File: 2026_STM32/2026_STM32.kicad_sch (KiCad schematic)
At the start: 15 parts, among them J1 USB_B, J2 Conn_ARM_SWD_TagConnect_TC2030, SW1 1825910-6, U1 STM32C011J4Mx, U2 XC6206P332MR, U3 KTD2026

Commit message: Redo schematic for 20 pin STM and adding more LEDs
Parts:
- removed C4: 100n, Capacitor_SMD:C_0603_1608Metric_Pad1.08x0.95mm_HandSolder, symbol Device:C
- removed C5: C, Capacitor_SMD:C_0603_1608Metric_Pad1.08x0.95mm_HandSolder, symbol Device:C
- removed D2: BLUE, Diode_SMD:D_1206_3216Metric_Pad1.42x1.75mm_HandSolder, symbol Device:LED
- removed J2: Conn_ARM_SWD_TagConnect_TC2030, Connector:Tag-Connect_TC2030-IDC-FP_2x03_P1.27mm_Vertical, symbol Connector:Conn_ARM_SWD_TagConnect_TC2030
- removed R1: 100R, Capacitor_SMD:C_0603_1608Metric_Pad1.08x0.95mm_HandSolder, symbol Device:R_US
- removed RV1: TC33X-2-203E, Potentiometer_SMD:Potentiometer_Bourns_TC33X_Vertical, symbol Device:R_Potentiometer
- removed SW1: 1825910-6, Button_Switch_THT:SW_PUSH_6mm, symbol Switch:SW_Push
- removed U1: STM32C011J4Mx, Package_SO:SOIC-8_3.9x4.9mm_P1.27mm, symbol MCU_ST_STM32C0:STM32C011J4Mx
- added C6: 100nF, Capacitor_SMD:C_0603_1608Metric_Pad1.08x0.95mm_HandSolder, symbol Device:C
- added C7: 4.7uF, Capacitor_SMD:C_0603_1608Metric_Pad1.08x0.95mm_HandSolder, symbol Device:C
- added D3: RED, Diode_SMD:D_1206_3216Metric_Pad1.42x1.75mm_HandSolder, symbol Device:LED
- added D4: GREEN, Diode_SMD:D_1206_3216Metric_Pad1.42x1.75mm_HandSolder, symbol Device:LED
- added D5: BLUE, Diode_SMD:D_1206_3216Metric_Pad1.42x1.75mm_HandSolder, symbol Device:LED
- added J3: Conn_01x05_Pin, symbol Connector:Conn_01x05_Pin
- added R2: 10kR, Capacitor_SMD:C_0603_1608Metric_Pad1.08x0.95mm_HandSolder, symbol Device:R_US
- added R3, R4, R5: 100R, Capacitor_SMD:C_0603_1608Metric_Pad1.08x0.95mm_HandSolder, symbol Device:R_US
- added RV2: TC33X-2-203E, Potentiometer_SMD:Potentiometer_Bourns_TC33X_Vertical, symbol Device:R_Potentiometer
- added SW2: 1825910-6, Button_Switch_THT:SW_PUSH_6mm, symbol Switch:SW_Push
- added U4: STM32C011F4P6, Package_SO:TSSOP-20_4.4x6.5mm_P0.65mm, symbol MCU_ST_STM32C0:STM32C011F4Px
- C3: value 100n -> 1.0uF
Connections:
- net +3V3: now also C6.1, C7.1, J3.1 (Pin_1), RV2.1, SW2.2, U4.4 (VDD)
- net GND: now also C6.2, C7.2, J3.5 (Pin_5), R2.2, R3.2, R4.2, R5.2, RV2.3, U4.5 (VSS)
- net SCL: now also U4.20 (PB6)
- net SDA: now also U4.1 (PB7)
- net SWDIO: now also J3.4 (Pin_4), U4.18 (PA13)
- net ~{RST}: now also J3.2 (Pin_2), U4.6 (PF2)
- new net: R2.1, SW2.1, U4.8 (PA1)
- new net: RV2.2, U4.7 (PA0)
- new net: D4.1 (K), R4.1
- new net: D5.1 (K), R5.1
- new net: D3.1 (K), R3.1
- new net BLUE: D5.2 (A), U4.11 (PA4)
- new net GREEN: D4.2 (A), U4.10 (PA3)
- new net RED: D3.2 (A), U4.9 (PA2)
- new net SWCLK: J3.3 (Pin_3), U4.19 (PA14)
- no-connect marks 4 -> 11
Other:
- company: (none) -> Waterloo Rocketry
- title: (none) -> 2026 Tutorial Board
- moved on the sheet: C3, D1, U3

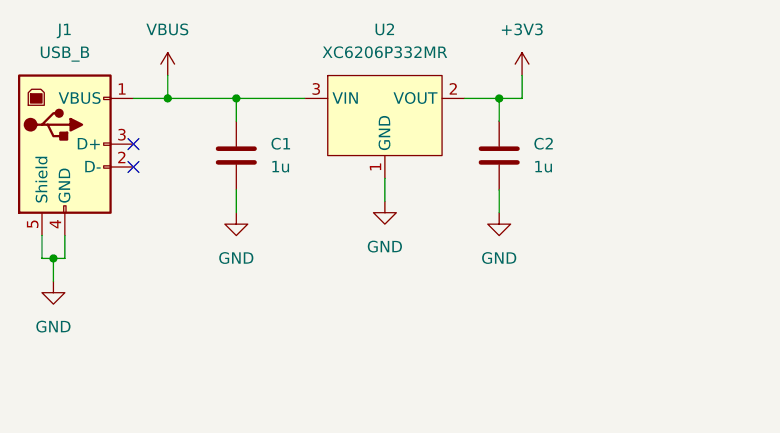
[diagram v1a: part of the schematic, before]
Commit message: Change LDO to SPX3819 (Existing Standard LDO)
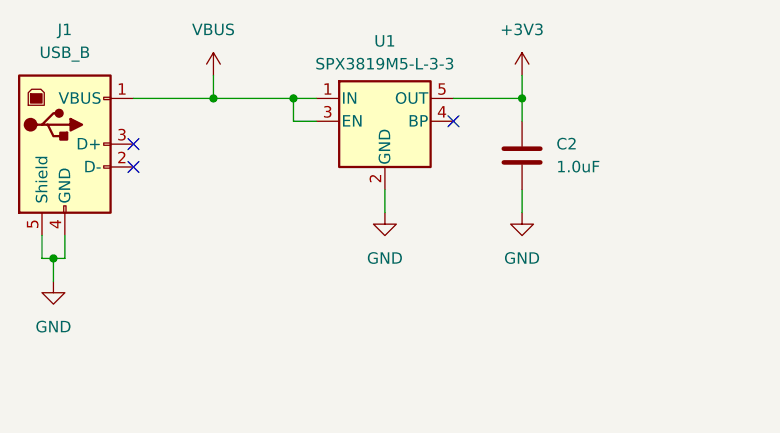
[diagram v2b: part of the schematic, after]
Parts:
- removed C1: 1u, Capacitor_SMD:C_0603_1608Metric_Pad1.08x0.95mm_HandSolder, symbol Device:C
- removed U2: XC6206P332MR, Package_TO_SOT_SMD:SOT-23_Handsoldering, symbol 2026-stm32:XC6206P332MR
- added U1: SPX3819M5-L-3-3, Package_TO_SOT_SMD:SOT-23-5, symbol Regulator_Linear:SPX3819M5-L-3-3
- C2: value 1u -> 1.0uF
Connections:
- net +3V3: now also U1.5 (OUT)
- net GND: now also U1.2 (GND)
- net VBUS: now also U1.1 (IN), U1.3 (EN)
- no-connect marks 11 -> 12
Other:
- moved on the sheet: C2

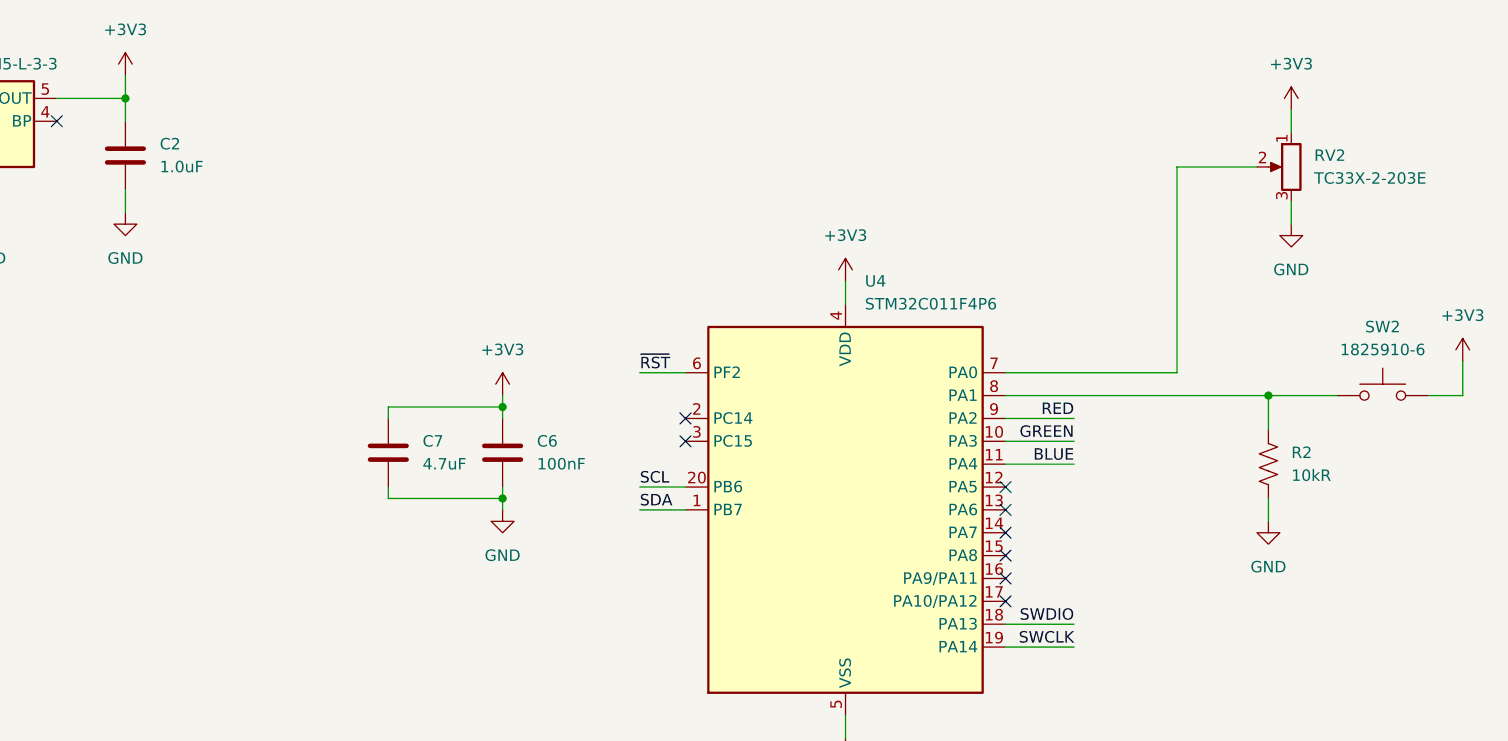
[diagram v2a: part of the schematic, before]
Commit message: added test points to SCL, SDA, potentiometer
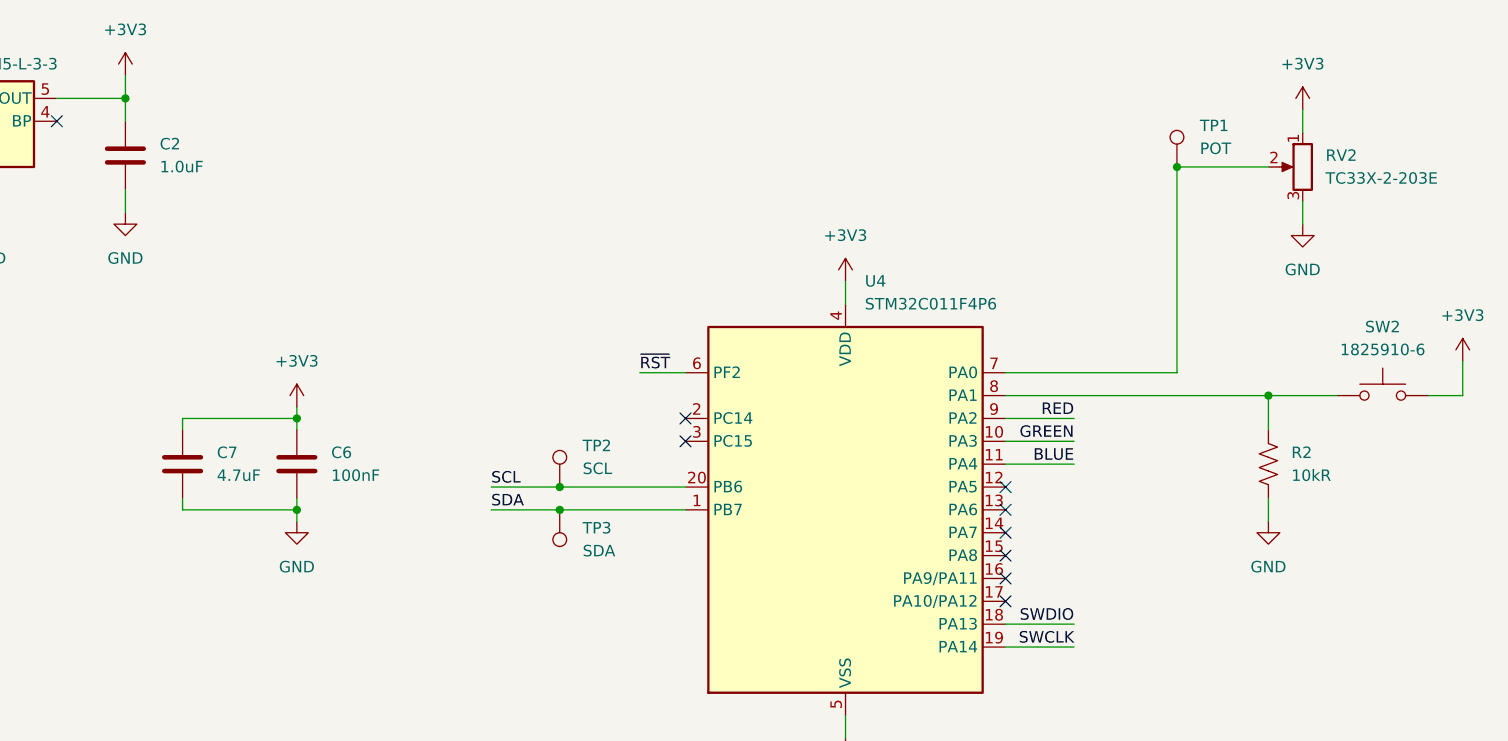
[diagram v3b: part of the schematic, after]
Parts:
- added TP1: POT, symbol Connector:TestPoint
- added TP2: SCL, symbol Connector:TestPoint
- added TP3: SDA, symbol Connector:TestPoint
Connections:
- net SCL: now also TP2.1
- net SDA: now also TP3.1
- net at RV2.2, U4.7 (PA0): now also TP1.1
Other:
- moved on the sheet: C6, C7, RV2

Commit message: Footprints and layout, need to do routing
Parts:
- C1: renamed from C2; footprint Capacitor_SMD:C_0603_1608Metric_Pad1.08x0.95mm_HandSolder -> Capacitor_SMD:C_0805_2012Metric_Pad1.18x1.45mm_HandSolder
- C2: renamed from C6; footprint Capacitor_SMD:C_0603_1608Metric_Pad1.08x0.95mm_HandSolder -> Capacitor_SMD:C_0805_2012Metric_Pad1.18x1.45mm_HandSolder
- C3: renamed from C7; footprint Capacitor_SMD:C_0603_1608Metric_Pad1.08x0.95mm_HandSolder -> Capacitor_SMD:C_0805_2012Metric_Pad1.18x1.45mm_HandSolder
- C4: renamed from C3; footprint Capacitor_SMD:C_0603_1608Metric_Pad1.08x0.95mm_HandSolder -> Capacitor_SMD:C_0805_2012Metric_Pad1.18x1.45mm_HandSolder
- J1: footprint (none) -> 2026 tutorial:CONN_USBB_12P04X10P62_AMP
- J2: renamed from J3; footprint (none) -> Connector_PinHeader_2.54mm:PinHeader_1x05_P2.54mm_Vertical
- R1: renamed from R2; footprint Capacitor_SMD:C_0603_1608Metric_Pad1.08x0.95mm_HandSolder -> Capacitor_SMD:C_0805_2012Metric_Pad1.18x1.45mm_HandSolder
- R2: renamed from R3; footprint Capacitor_SMD:C_0603_1608Metric_Pad1.08x0.95mm_HandSolder -> Capacitor_SMD:C_0805_2012Metric_Pad1.18x1.45mm_HandSolder
- R3: renamed from R4; footprint Capacitor_SMD:C_0603_1608Metric_Pad1.08x0.95mm_HandSolder -> Capacitor_SMD:C_0805_2012Metric_Pad1.18x1.45mm_HandSolder
- R4: renamed from R5; footprint Capacitor_SMD:C_0603_1608Metric_Pad1.08x0.95mm_HandSolder -> Capacitor_SMD:C_0805_2012Metric_Pad1.18x1.45mm_HandSolder
- TP1, TP2, TP3: footprint (none) -> TestPoint:TestPoint_Pad_D2.5mm
- renumbered D3 to D2, D4 to D3, D5 to D4, RV2 to RV1, SW2 to SW1, U4 to U2
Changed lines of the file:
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@@
 		(dnp no)
 		(fields_autoplaced yes)
-		(property "Reference" "C2"
+		(property "Reference" "C1"
 			(at 81.28 33.0199 0)
 			(effects
@@
 			)
 		)
-		(property "Footprint" "Capacitor_SMD:C_0603_1608Metric_Pad1.08x0.95mm_HandSolder"
+		(property "Footprint" "Capacitor_SMD:C_0805_2012Metric_Pad1.18x1.45mm_HandSolder"
 			(at 78.4352 38.1 0)
 			(effects
@@
 			(project "2026_STM32"
 				(path "/dd574f06-dff2-4225-9fdd-7ead27d41326"
-					(reference "C2")
+					(reference "C1")
 					(unit 1)
 				)
@@
 		(dnp no)
 		(fields_autoplaced yes)
-		(property "Reference" "R2"
+		(property "Reference" "R1"
 			(at 207.01 67.3099 0)
 			(effects
@@
 			)
 		)
-		(property "Footprint" "Capacitor_SMD:C_0603_1608Metric_Pad1.08x0.95mm_HandSolder"
+		(property "Footprint" "Capacitor_SMD:C_0805_2012Metric_Pad1.18x1.45mm_HandSolder"
 			(at 205.486 68.834 90)
 			(effects
@@
 			(project "2026_STM32"
 				(path "/dd574f06-dff2-4225-9fdd-7ead27d41326"
-					(reference "R2")
+					(reference "R1")
 					(unit 1)
 				)
@@
 			)
 		)
-		(property "Footprint" ""
+		(property "Footprint" "TestPoint:TestPoint_Pad_D2.5mm"
 			(at 130.81 71.12 0)
 			(effects
@@
 		(dnp no)
 		(fields_autoplaced yes)
-		(property "Reference" "RV2"
+		(property "Reference" "RV1"
 			(at 210.82 34.2899 0)
 			(effects
@@
 			(project "2026_STM32"
 				(path "/dd574f06-dff2-4225-9fdd-7ead27d41326"
-					(reference "RV2")
+					(reference "RV1")
 					(unit 1)
 				)
@@
 			)
 		)
-		(property "Footprint" ""
+		(property "Footprint" "2026 tutorial:CONN_USBB_12P04X10P62_AMP"
 			(at 30.48 34.29 0)
 			(effects
@@
 		(dnp no)
 		(fields_autoplaced yes)
-		(property "Reference" "SW2"
+		(property "Reference" "SW1"
 			(at 217.17 53.34 0)
 			(effects
@@
 			(project "2026_STM32"
 				(path "/dd574f06-dff2-4225-9fdd-7ead27d41326"
-					(reference "SW2")
+					(reference "SW1")
 					(unit 1)
 				)
@@
 		(dnp no)
 		(fields_autoplaced yes)
-		(property "Reference" "R4"
+		(property "Reference" "R3"
 			(at 139.7 137.1599 0)
 			(effects
@@
 			)
 		)
-		(property "Footprint" "Capacitor_SMD:C_0603_1608Metric_Pad1.08x0.95mm_HandSolder"
+		(property "Footprint" "Capacitor_SMD:C_0805_2012Metric_Pad1.18x1.45mm_HandSolder"
 			(at 138.176 138.684 90)
 			(effects
@@
 			(project "2026_STM32"
 				(path "/dd574f06-dff2-4225-9fdd-7ead27d41326"
-					(reference "R4")
+					(reference "R3")
 					(unit 1)
 				)
@@
 		(dnp no)
 		(fields_autoplaced yes)
-		(property "Reference" "D5"
+		(property "Reference" "D4"
 			(at 153.67 128.5874 90)
 			(effects
@@
 			(project "2026_STM32"
 				(path "/dd574f06-dff2-4225-9fdd-7ead27d41326"
-					(reference "D5")
+					(reference "D4")
 					(unit 1)
 				)
@@
 		(on_board yes)
 		(dnp no)
-		(property "Reference" "C7"
+		(property "Reference" "C3"
 			(at 87.63 67.3099 0)
 			(effects
@@
 			)
 		)
-		(property "Footprint" "Capacitor_SMD:C_0603_1608Metric_Pad1.08x0.95mm_HandSolder"
+		(property "Footprint" "Capacitor_SMD:C_0805_2012Metric_Pad1.18x1.45mm_HandSolder"
 			(at 84.7852 72.39 0)
 			(effects
@@
 			(project "2026_STM32"
 				(path "/dd574f06-dff2-4225-9fdd-7ead27d41326"
-					(reference "C7")
+					(reference "C3")
 					(unit 1)
 				)
@@
 		(dnp no)
 		(fields_autoplaced yes)
-		(property "Reference" "U4"
+		(property "Reference" "U2"
 			(at 159.6233 48.26 0)
 			(effects
@@
 			(project ""
 				(path "/dd574f06-dff2-4225-9fdd-7ead27d41326"
-					(reference "U4")
+					(reference "U2")
 					(unit 1)
 				)
@@
 		(dnp no)
 		(fields_autoplaced yes)
-		(property "Reference" "D4"
+		(property "Reference" "D3"
 			(at 140.97 128.5874 90)
 			(effects
@@
 			(project "2026_STM32"
 				(path "/dd574f06-dff2-4225-9fdd-7ead27d41326"
-					(reference "D4")
+					(reference "D3")
 					(unit 1)
 				)
@@
 			)
 		)
-		(property "Footprint" ""
+		(property "Footprint" "TestPoint:TestPoint_Pad_D2.5mm"
 			(at 120.65 73.66 0)
 			(effects
@@
 			)
 		)
-		(property "Footprint" ""
+		(property "Footprint" "TestPoint:TestPoint_Pad_D2.5mm"
 			(at 199.39 35.56 0)
 			(effects
@@
 		(dnp no)
 		(fields_autoplaced yes)
-		(property "Reference" "R3"
+		(property "Reference" "R2"
 			(at 128.27 137.1599 0)
 			(effects
@@
 			)
 		)
-		(property "Footprint" "Capacitor_SMD:C_0603_1608Metric_Pad1.08x0.95mm_HandSolder"
+		(property "Footprint" "Capacitor_SMD:C_0805_2012Metric_Pad1.18x1.45mm_HandSolder"
 			(at 126.746 138.684 90)
 			(effects
@@
 			(project "2026_STM32"
 				(path "/dd574f06-dff2-4225-9fdd-7ead27d41326"
-					(reference "R3")
+					(reference "R2")
 					(unit 1)
 				)
@@
 		(dnp no)
 		(fields_autoplaced yes)
-		(property "Reference" "C6"
+		(property "Reference" "C2"
 			(at 100.33 67.3099 0)
 			(effects
@@
 			)
 		)
-		(property "Footprint" "Capacitor_SMD:C_0603_1608Metric_Pad1.08x0.95mm_HandSolder"
+		(property "Footprint" "Capacitor_SMD:C_0805_2012Metric_Pad1.18x1.45mm_HandSolder"
 			(at 97.4852 72.39 0)
 			(effects
@@
 			(project "2026_STM32"
 				(path "/dd574f06-dff2-4225-9fdd-7ead27d41326"
-					(reference "C6")
+					(reference "C2")
 					(unit 1)
 				)
@@
 		(dnp no)
 		(fields_autoplaced yes)
-		(property "Reference" "D3"
+		(property "Reference" "D2"
 			(at 129.54 128.5874 90)
 			(effects
@@
 			(project "2026_STM32"
 				(path "/dd574f06-dff2-4225-9fdd-7ead27d41326"
-					(reference "D3")
+					(reference "D2")
 					(unit 1)
 				)
@@
 		(dnp no)
 		(fields_autoplaced yes)
-		(property "Reference" "R5"
+		(property "Reference" "R4"
 			(at 152.4 137.1599 0)
 			(effects
@@
 			)
 		)
-		(property "Footprint" "Capacitor_SMD:C_0603_1608Metric_Pad1.08x0.95mm_HandSolder"
+		(property "Footprint" "Capacitor_SMD:C_0805_2012Metric_Pad1.18x1.45mm_HandSolder"
 			(at 150.876 138.684 90)
 			(effects
@@
 			(project "2026_STM32"
 				(path "/dd574f06-dff2-4225-9fdd-7ead27d41326"
-					(reference "R5")
+					(reference "R4")
 					(unit 1)
 				)
@@
 		(dnp no)
 		(fields_autoplaced yes)
-		(property "Reference" "J3"
+		(property "Reference" "J2"
 			(at 45.085 71.12 0)
 			(effects
@@
 			)
 		)
-		(property "Footprint" ""
+		(property "Footprint" "Connector_PinHeader_2.54mm:PinHeader_1x05_P2.54mm_Vertical"
 			(at 44.45 81.28 0)
 			(effects
@@
 			(project ""
 				(path "/dd574f06-dff2-4225-9fdd-7ead27d41326"
-					(reference "J3")
+					(reference "J2")
 					(unit 1)
 				)
@@
 		(dnp no)
 		(fields_autoplaced yes)
-		(property "Reference" "C3"
+		(property "Reference" "C4"
 			(at 83.82 134.6199 0)
 			(effects
@@
 			)
 		)
-		(property "Footprint" "Capacitor_SMD:C_0603_1608Metric_Pad1.08x0.95mm_HandSolder"
+		(property "Footprint" "Capacitor_SMD:C_0805_2012Metric_Pad1.18x1.45mm_HandSolder"
 			(at 80.9752 139.7 0)
 			(effects
@@
 			(project "2026_STM32"
 				(path "/dd574f06-dff2-4225-9fdd-7ead27d41326"
-					(reference "C3")
+					(reference "C4")
 					(unit 1)
 				)

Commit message: stuff
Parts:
- removed D1: CLX6F-FKC, LED_SMD:LED_RGB_PLCC-6, symbol LED:CLX6F-FKC
- removed U3: KTD2026, Package_DFN_QFN:DFN-8-1EP_1.5x1.5mm_P0.4mm_EP0.7x1.2mm, symbol Driver_LED:KTD2026
- added C5: 100nF, Capacitor_SMD:C_0805_2012Metric_Pad1.18x1.45mm_HandSolder, symbol Device:C
- added F1: 0.5A, Fuse:Fuse_0805_2012Metric_Pad1.15x1.40mm_HandSolder, symbol Device:Polyfuse
- added J3: USB_C_Receptacle_USB2.0_16P, Connector_USB:USB_C_Receptacle_GCT_USB4105-xx-A_16P_TopMnt_Horizontal, symbol Connector:USB_C_Receptacle_USB2.0_16P
- added R10: 330R, Capacitor_SMD:C_0805_2012Metric_Pad1.18x1.45mm_HandSolder, symbol Device:R_US
- added R5, R6, R7: 10kR, Capacitor_SMD:C_0805_2012Metric_Pad1.18x1.45mm_HandSolder, symbol Device:R_US
- added R8, R9: 5.1kR, Capacitor_SMD:C_0805_2012Metric_Pad1.18x1.45mm_HandSolder, symbol Device:R_US
- added TP4: TX, TestPoint:TestPoint_THTPad_D2.5mm_Drill1.2mm, symbol Connector:TestPoint
- added TP5: RX, TestPoint:TestPoint_THTPad_D2.5mm_Drill1.2mm, symbol Connector:TestPoint
- added U4: CH340N, Package_SO:JEITA_SOIC-8_3.9x4.9mm_P1.27mm, symbol Interface_USB:CH340N
- added U5: TMP1075DSG, Package_SON:WSON-8-1EP_2x2mm_P0.5mm_EP0.9x1.6mm_ThermalVias, symbol Sensor_Temperature:TMP1075DSG
- C1: value 1.0uF -> 4.7uF
- C4: value 1.0uF -> 100nF
- J1: now not fitted
- R2: value 100R -> 330R
- RV1: footprint Potentiometer_SMD:Potentiometer_Bourns_TC33X_Vertical -> 2026 tutorial:PTV09A4015UB103
- SW1: LCSC (none) -> C428628
- TP1, TP2, TP3: footprint TestPoint:TestPoint_Pad_D2.5mm -> TestPoint:TestPoint_THTPad_D2.5mm_Drill1.2mm
- U2: LCSC (none) -> C7373263
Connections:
- net +3V3: now also D2.2 (A), D3.2 (A), D4.2 (A), C5.1, R5.1, R6.1, R7.1, U4.5 (VCC), U4.8 (V3), U5.8 (V+)
- net BLUE: now also R4.2; no longer D4.2 (A)
- net GND: now also C5.2, J3.A1 (GND), J3.A12 (GND), J3.B1 (GND), J3.B12 (GND), J3.SH (SHIELD), R8.2, R9.2, U4.3 (GND), U5.4 (GND), U5.5 (A2), U5.6 (A1), U5.7 (A0), U5.9 (EP); no longer R2.2, R3.2, R4.2
- net GREEN: now also R3.2; no longer D3.2 (A)
- net RED: now also R2.2; no longer D2.2 (A)
- net SCL: now also R5.2, U5.2 (SCL)
- net SDA: now also R6.2, U5.1 (SDA)
- net VBUS: now also F1.2; no longer J1.1 (VBUS)
- net at R1.1, SW1.1: now also U2.15 (PA8); no longer U2.8 (PA1)
- net at RV1.2, TP1.1: now also R10.2; no longer U2.7 (PA0)
- net at U2.13 (PA6): now also R10.1
- new net: J3.A6 (D+), J3.B6 (D+), U4.1 (UD+)
- new net: J3.A7 (D-), J3.B7 (D-), U4.2 (UD-)
- new net: F1.1, J1.1 (VBUS), J3.A4 (VBUS), J3.A9 (VBUS), J3.B4 (VBUS), J3.B9 (VBUS)
- new net: J3.A5 (CC1), R9.1
- new net: J3.B5 (CC2), R8.1
- new net ALERT: R7.2, U5.3 (ALERT)
- new net MCU_RX: TP5.1, U2.8 (PA1), U4.6 (TXD)
- new net MCU_TX: TP4.1, U2.7 (PA0), U4.7 (RXD)
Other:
- moved on the sheet: C2, C3, D2, D3, D4, J2, R2, R3, R4, TP2, TP3, U2

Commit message: done
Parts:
- removed J1: USB_B, 2026 tutorial:CONN_USBB_12P04X10P62_AMP, symbol Connector:USB_B
- removed TP4: TX, TestPoint:TestPoint_THTPad_D2.5mm_Drill1.2mm, symbol Connector:TestPoint
- removed TP5: RX, TestPoint:TestPoint_THTPad_D2.5mm_Drill1.2mm, symbol Connector:TestPoint
- added H1, H2: MountingHole_Pad, MountingHole:MountingHole_3.2mm_M3_Pad, symbol Mechanical:MountingHole_Pad
- added R11: 330R, Capacitor_SMD:C_0805_2012Metric_Pad1.18x1.45mm_HandSolder, symbol Device:R_US
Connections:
- net ALERT is gone; now on net Alert: R7.2, U5.3 (ALERT)
- net GND: now also J2.3 (Pin_3), H1.1, H2.1; no longer J2.5 (Pin_5)
- net SWCLK: now also J2.4 (Pin_4); no longer J2.3 (Pin_3)
- net SWDIO: now also J2.5 (Pin_5); no longer J2.4 (Pin_4)
- net at R1.1, SW1.1: now also R11.1; no longer U2.15 (PA8)
- net Alert: now reaches U2.2 (PC14)
- new net: R11.2, U2.15 (PA8)
- no-connect marks 12 -> 9
